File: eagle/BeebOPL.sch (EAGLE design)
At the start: 38 parts, among them IC1 LM324N, IC2 YM3014B, IC5 74LS02N, IC6 YM3812, IC7 74LS04N, IC9 74HCT688N, J1 1 MHz Bus, J2 Feed-through, J3 3.5mm Jack, J4 5V DC

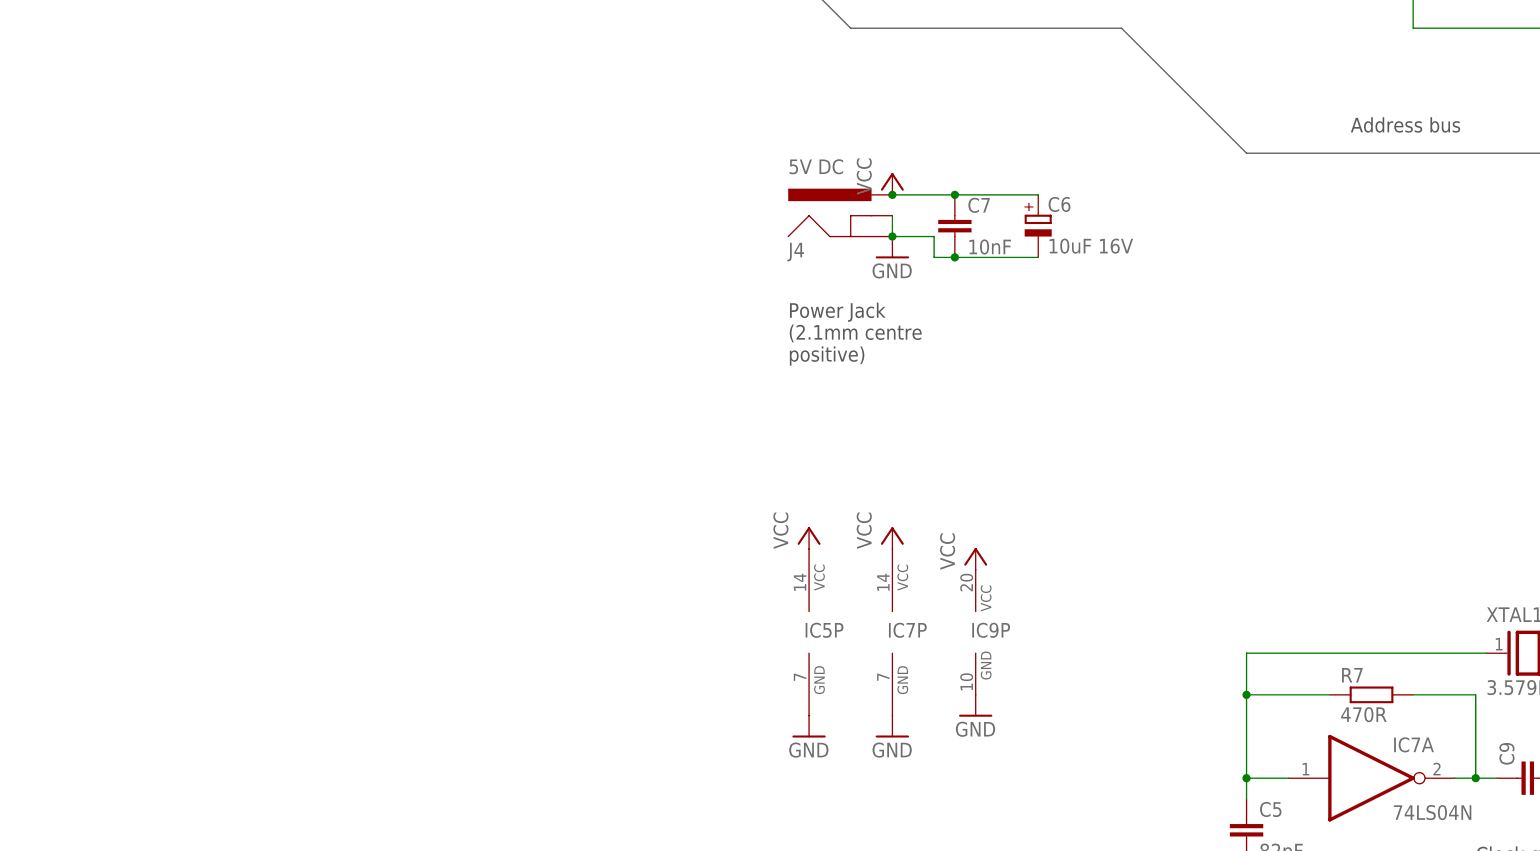
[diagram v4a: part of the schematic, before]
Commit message: Added optional power regualtor
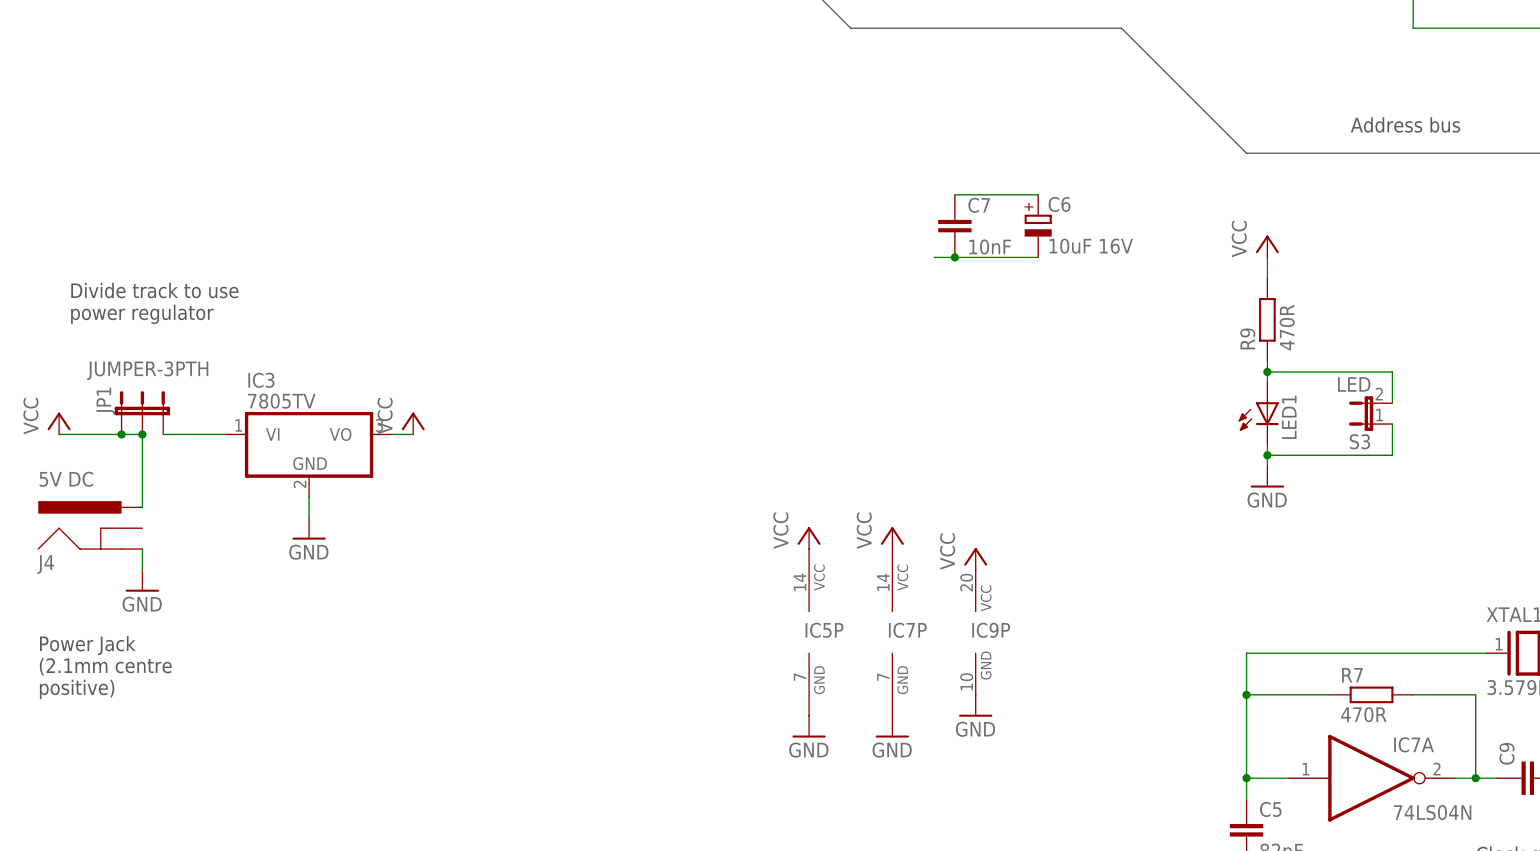
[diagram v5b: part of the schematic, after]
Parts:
- added IC3: 7805TV, linear:7805TV
- added JP1: JUMPER-3PTH, SparkFun-Retired:JUMPER-3PTH
- added LED1: (no value), led:LED5MM
- added R9: 470R, resistor:R-EU_0207/10
- added S3: LED, SparkFun-Retired:JUMPER-2PTH
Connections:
- new net N$25: LED1.A, R9.1, S3.2
- new net N$27: IC3.VI, JP1.3
- new net N$28: C6.-, C7.2
- new net N$29: C6.+, C7.1
- net GND: now also IC3.GND, LED1.C, S3.1; no longer C6.-, C7.2, J4.GNDBREAK
- net VCC: now also IC3.VO, JP1.1, JP1.2, R9.2; no longer C6.+, C7.1
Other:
- note added: "Divide track to use power regulator"
- moved on the sheet: J4
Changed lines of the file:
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@@
 <setting verticaltext="up"/>
 </settings>
-<grid distance="0.1" unitdist="inch" unit="inch" style="lines" multiple="1" display="no" altdistance="0.01" altunitdist="inch" altunit="inch"/>
+<grid distance="0.05" unitdist="inch" unit="inch" style="lines" multiple="1" display="no" altdistance="0.01" altunitdist="inch" altunit="inch"/>
 <layers>
 <layer number="1" name="Top" color="4" fill="1" visible="no" active="no"/>
@@
 <part name="GND12" library="supply1" deviceset="GND" device=""/>
 <part name="J4" library="SparkFun-Connectors" deviceset="POWER_JACK" device="SLT" value="5V DC"/>
-<part name="GND13" library="supply1" deviceset="GND" device=""/>
-<part name="P+7" library="supply1" deviceset="VCC" device=""/>
 <part name="P+1" library="supply1" deviceset="VCC" device=""/>
 <part name="S1" library="SparkFun-Retired" deviceset="JUMPER-2" device="PTH" value="1MHz Bus Audio"/>
@@
 <part name="P+2" library="supply1" deviceset="VCC" device=""/>
 <part name="GND3" library="supply1" deviceset="GND" device=""/>
+<part name="S3" library="SparkFun-Retired" deviceset="JUMPER-2" device="PTH" value="LED"/>
+<part name="LED1" library="led" deviceset="LED" device="5MM"/>
+<part name="R9" library="resistor" deviceset="R-EU_" device="0207/10" value="470R"/>
+<part name="P+8" library="supply1" deviceset="VCC" device=""/>
+<part name="GND14" library="supply1" deviceset="GND" device=""/>
+<part name="IC3" library="linear" deviceset="78*" device="TV" technology="05"/>
+<part name="GND17" library="supply1" deviceset="GND" device=""/>
+<part name="P+11" library="supply1" deviceset="VCC" device=""/>
+<part name="JP1" library="SparkFun-Retired" deviceset="JUMPER-3" device="PTH"/>
+<part name="P+12" library="supply1" deviceset="VCC" device=""/>
+<part name="GND13" library="supply1" deviceset="GND" device=""/>
 </parts>
 <sheets>
@@
 addresses &amp;FC04
 and &amp;FC05)</text>
-<text x="-185.42" y="40.64" size="1.778" layer="97">Power Jack
+<text x="-276.86" y="0" size="1.778" layer="97">Power Jack
 (2.1mm centre
 positive)</text>
@@
 (Richard Watts &amp; Music Sales Limited, 1985)</text>
 <frame x1="-198.12" y1="-139.7" x2="200.66" y2="157.48" columns="8" rows="5" layer="91"/>
+<text x="-273.05" y="45.72" size="1.778" layer="97">Divide track to use
+power regulator</text>
 </plain>
 <instances>
@@
 <instance part="P+6" gate="VCC" x="-182.88" y="20.32"/>
 <instance part="GND12" gate="1" x="-182.88" y="-5.08"/>
-<instance part="J4" gate="G$1" x="-175.26" y="53.34"/>
-<instance part="GND13" gate="1" x="-172.72" y="53.34"/>
-<instance part="P+7" gate="VCC" x="-172.72" y="63.5"/>
+<instance part="J4" gate="G$1" x="-266.7" y="15.24"/>
 <instance part="P+1" gate="VCC" x="91.44" y="5.08"/>
 <instance part="S1" gate="A" x="172.72" y="-63.5" rot="R90"/>
@@
 <instance part="P+2" gate="VCC" x="127" y="81.28"/>
 <instance part="GND3" gate="1" x="127" y="20.32"/>
+<instance part="S3" gate="A" x="-114.3" y="33.02" rot="R90"/>
+<instance part="LED1" gate="G$1" x="-127" y="35.56"/>
+<instance part="R9" gate="G$1" x="-127" y="45.72" rot="R90"/>
+<instance part="P+8" gate="VCC" x="-127" y="55.88"/>
+<instance part="GND14" gate="1" x="-127" y="25.4"/>
+<instance part="IC3" gate="A1" x="-243.84" y="31.75"/>
+<instance part="GND17" gate="1" x="-243.84" y="19.05"/>
+<instance part="P+11" gate="VCC" x="-231.14" y="34.29"/>
+<instance part="JP1" gate="G$1" x="-266.7" y="34.29" smashed="yes">
+<attribute name="NAME" x="-267.97" y="34.29" size="1.778" layer="95" rot="R90"/>
+<attribute name="VALUE" x="-255.905" y="40.64" size="1.778" layer="96" rot="R180"/>
+</instance>
+<instance part="P+12" gate="VCC" x="-274.32" y="34.29"/>
+<instance part="GND13" gate="1" x="-264.16" y="12.7"/>
 </instances>
 <busses>
@@
 <pinref part="IC5" gate="P" pin="GND"/>
 <pinref part="GND12" gate="1" pin="GND"/>
-</segment>
-<segment>
-<pinref part="J4" gate="G$1" pin="GNDBREAK"/>
-<pinref part="J4" gate="G$1" pin="GND"/>
-<wire x1="-172.72" y1="58.42" x2="-172.72" y2="55.88" width="0.1524" layer="91"/>
-<pinref part="GND13" gate="1" pin="GND"/>
-<junction x="-172.72" y="55.88"/>
-<wire x1="-172.72" y1="55.88" x2="-167.64" y2="55.88" width="0.1524" layer="91"/>
-<wire x1="-167.64" y1="55.88" x2="-167.64" y2="53.34" width="0.1524" layer="91"/>
-<wire x1="-167.64" y1="53.34" x2="-165.1" y2="53.34" width="0.1524" layer="91"/>
-<pinref part="C6" gate="G$1" pin="-"/>
-<wire x1="-165.1" y1="53.34" x2="-154.94" y2="53.34" width="0.1524" layer="91"/>
-<pinref part="C7" gate="G$1" pin="2"/>
-<junction x="-165.1" y="53.34"/>
 </segment>
 <segment>
@@
 <junction x="127" y="22.86"/>
 </segment>
+<segment>
+<pinref part="GND14" gate="1" pin="GND"/>
+<pinref part="LED1" gate="G$1" pin="C"/>
+<wire x1="-127" y1="27.94" x2="-127" y2="29.21" width="0.1524" layer="91"/>
+<pinref part="S3" gate="A" pin="1"/>
+<wire x1="-127" y1="29.21" x2="-127" y2="30.48" width="0.1524" layer="91"/>
+<wire x1="-111.76" y1="33.02" x2="-111.76" y2="29.21" width="0.1524" layer="91"/>
+<wire x1="-111.76" y1="29.21" x2="-127" y2="29.21" width="0.1524" layer="91"/>
+<junction x="-127" y="29.21"/>
+</segment>
+<segment>
+<pinref part="IC3" gate="A1" pin="GND"/>
+<pinref part="GND17" gate="1" pin="GND"/>
+<wire x1="-243.84" y1="24.13" x2="-243.84" y2="21.59" width="0.1524" layer="91"/>
+</segment>
+<segment>
+<pinref part="J4" gate="G$1" pin="GND"/>
+<wire x1="-264.16" y1="17.78" x2="-264.16" y2="15.24" width="0.1524" layer="91"/>
+<pinref part="GND13" gate="1" pin="GND"/>
+</segment>
 </net>
 <net name="D0" class="0">
@@
 <pinref part="IC5" gate="P" pin="VCC"/>
 <pinref part="P+6" gate="VCC" pin="VCC"/>
-</segment>
-<segment>
-<pinref part="J4" gate="G$1" pin="PWR"/>
-<pinref part="P+7" gate="VCC" pin="VCC"/>
-<wire x1="-172.72" y1="60.96" x2="-165.1" y2="60.96" width="0.1524" layer="91"/>
-<junction x="-172.72" y="60.96"/>
-<pinref part="C7" gate="G$1" pin="1"/>
-<wire x1="-165.1" y1="60.96" x2="-154.94" y2="60.96" width="0.1524" layer="91"/>
-<junction x="-165.1" y="60.96"/>
-<pinref part="C6" gate="G$1" pin="+"/>
 </segment>
 <segment>
@@
 <pinref part="P+2" gate="VCC" pin="VCC"/>
 <junction x="127" y="78.74"/>
+</segment>
+<segment>
+<pinref part="R9" gate="G$1" pin="2"/>
+<pinref part="P+8" gate="VCC" pin="VCC"/>
+<wire x1="-127" y1="50.8" x2="-127" y2="53.34" width="0.1524" layer="91"/>
+</segment>
+<segment>
+<pinref part="IC3" gate="A1" pin="VO"/>
+<wire x1="-233.68" y1="31.75" x2="-231.14" y2="31.75" width="0.1524" layer="91"/>
+<pinref part="P+11" gate="VCC" pin="VCC"/>
+</segment>
+<segment>
+<pinref part="JP1" gate="G$1" pin="1"/>
+<wire x1="-266.7" y1="31.75" x2="-274.32" y2="31.75" width="0.1524" layer="91"/>
+<pinref part="P+12" gate="VCC" pin="VCC"/>
+<pinref part="JP1" gate="G$1" pin="2"/>
+<wire x1="-266.7" y1="31.75" x2="-264.16" y2="31.75" width="0.1524" layer="91"/>
+<junction x="-266.7" y="31.75"/>
+<pinref part="J4" gate="G$1" pin="PWR"/>
+<wire x1="-264.16" y1="22.86" x2="-264.16" y2="31.75" width="0.1524" layer="91"/>
+<junction x="-264.16" y="31.75"/>
 </segment>
 </net>
@@
 </segment>
 </net>
+<net name="N$25" class="0">
+<segment>
+<pinref part="LED1" gate="G$1" pin="A"/>
+<pinref part="R9" gate="G$1" pin="1"/>
+<wire x1="-127" y1="38.1" x2="-127" y2="39.37" width="0.1524" layer="91"/>
+<wire x1="-127" y1="39.37" x2="-127" y2="40.64" width="0.1524" layer="91"/>
+<wire x1="-127" y1="39.37" x2="-111.76" y2="39.37" width="0.1524" layer="91"/>
+<junction x="-127" y="39.37"/>
+<pinref part="S3" gate="A" pin="2"/>
+<wire x1="-111.76" y1="39.37" x2="-111.76" y2="35.56" width="0.1524" layer="91"/>
+</segment>
+</net>
+<net name="N$27" class="0">
+<segment>
+<pinref part="JP1" gate="G$1" pin="3"/>
+<pinref part="IC3" gate="A1" pin="VI"/>
+<wire x1="-261.62" y1="31.75" x2="-254" y2="31.75" width="0.1524" layer="91"/>
+</segment>
+</net>
+<net name="N$29" class="1">
+<segment>
+<pinref part="C7" gate="G$1" pin="1"/>
+<wire x1="-165.1" y1="60.96" x2="-154.94" y2="60.96" width="0.1524" layer="91"/>
+<pinref part="C6" gate="G$1" pin="+"/>
+</segment>
+</net>
+<net name="N$28" class="3">
+<segment>
+<wire x1="-167.64" y1="53.34" x2="-165.1" y2="53.34" width="0.1524" layer="91"/>
+<pinref part="C6" gate="G$1" pin="-"/>
+<wire x1="-165.1" y1="53.34" x2="-154.94" y2="53.34" width="0.1524" layer="91"/>
+<pinref part="C7" gate="G$1" pin="2"/>
+<junction x="-165.1" y="53.34"/>
+</segment>
+</net>
